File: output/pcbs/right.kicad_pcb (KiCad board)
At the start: 2 copper layers, 115.8 x 102 mm, 69 parts

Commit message: added pcbs
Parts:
- removed the ? at (166.0, 136.5)
- removed the ? at (109.0, 140.8)
- removed the ? at (109.8, 87.5)
- removed the ? at (166.0, 83.2)
- removed the ? at (147.2, 113.8)
- added ?: , HOLE_M2_TH, F.Cu at (281.5, 136.5)
- added ?: , HOLE_M2_TH, F.Cu at (338.5, 140.8)
- added ?: , HOLE_M2_TH, F.Cu at (337.8, 87.5)
- added ?: , HOLE_M2_TH, F.Cu at (281.5, 83.2)
- added ?: , HOLE_M2_TH, F.Cu at (301.0, 118.8)
- moved D2 248.1 mm to (355.3, 135.8), turned to -90 degrees
- moved D3 248.1 mm to (355.3, 118.0), turned to -90 degrees
- moved D1 247.5 mm to (355.3, 153.5), turned to -90 degrees
- moved S1 247.5 mm to (347.5, 150.0)
- moved S2 247.5 mm to (347.5, 132.2)
- moved S3 247.5 mm to (347.5, 114.5)
- moved S4 247.5 mm to (347.5, 96.8)
- moved S5 247.5 mm to (347.5, 79.0)
- moved D4 234.9 mm to (355.3, 100.2), turned to -90 degrees
- moved D5 234.9 mm to (355.3, 82.5), turned to -90 degrees
- moved D26 234.5 mm to (336.6, 77.0), turned to -90 degrees
- moved D6 213.0 mm to (336.6, 153.5), turned to -90 degrees
- moved D7 210.7 mm to (336.6, 118.0), turned to -90 degrees
- moved D8 210.7 mm to (336.6, 100.2), turned to -90 degrees
- moved S10 210.0 mm to (328.8, 79.0)
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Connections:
- net first_mod renamed mirror_first_mod
- net sixth_bottom renamed mirror_sixth_bottom
- net sixth_mod renamed mirror_sixth_mod
- net sixth_top renamed mirror_sixth_top
- net third_bottom renamed mirror_third_bottom
- net third_mod renamed mirror_third_mod
- D11 pad 1: P029 -> P002
- D11 pad 2: third_top -> mirror_third_home
- D12 pad 1: P031 -> P029
- D12 pad 2: third_num -> mirror_third_top
- D13 pad 1: P115 -> P031
- D13 pad 2: fourth_bottom -> mirror_third_num
- D14 pad 1: P002 -> P113
- D14 pad 2: fourth_home -> mirror_fourth_mod
- D15 pad 1: P031 -> P115
- D15 pad 2: fourth_num -> mirror_fourth_bottom
- D16 pad 1: P113 -> P029
- D16 pad 2: fifth_mod -> mirror_fourth_top
- D17 pad 1: P115 -> P031
- D17 pad 2: fifth_bottom -> mirror_fourth_num
- D18 pad 1: P002 -> P113
- D18 pad 2: fifth_home -> mirror_fifth_mod
- D19 pad 1: P029 -> P002
- D19 pad 2: fifth_top -> mirror_fifth_home
- D2 pad 1: P002 -> P115
- D2 pad 2: first_home -> mirror_first_bottom
- D20 pad 1: P031 -> P029
- D20 pad 2: fifth_num -> mirror_fifth_top
- D23 pad 1: P031 -> P002
- D23 pad 2: sixth_num -> mirror_sixth_home
- D25 pad 1: P002 -> P115
- D25 pad 2: sixth_home -> mirror_second_bottom
- D26 pad 1: P115 -> P031
- D26 pad 2: first_bottom -> mirror_second_num
- D27 pad 1: P031 -> P002
- D27 pad 2: first_num -> mirror_fourth_home
- D28 pad 1: P002 -> P115
- D28 pad 2: third_home -> mirror_fifth_bottom
- D29 pad 1: P113 -> P031
- D29 pad 2: fourth_mod -> mirror_fifth_num
- D3 pad 1: P029 -> P002
- D3 pad 2: first_top -> mirror_first_home
- D30 pad 1: P029 -> P031
- D30 pad 2: fourth_top -> mirror_sixth_num
- D4 pad 1: P113 -> P029
- D4 pad 2: second_mod -> mirror_first_top
- D5 pad 1: P115 -> P031
- D5 pad 2: second_bottom -> mirror_first_num
- D6 pad 1: P002 -> P113
- D6 pad 2: second_home -> mirror_second_mod
- D7 pad 1: P029 -> P002
- D7 pad 2: second_top -> mirror_second_home
- D8 pad 1: P031 -> P029
- D8 pad 2: second_num -> mirror_second_top
- S10 pad 2: second_num -> mirror_second_num
- S13 pad 2: third_home -> mirror_third_home
- S14 pad 2: third_top -> mirror_third_top
- S15 pad 2: third_num -> mirror_third_num
- S16 pad 2: fourth_mod -> mirror_fourth_mod
- S17 pad 2: fourth_bottom -> mirror_fourth_bottom
- S18 pad 2: fourth_home -> mirror_fourth_home
- S19 pad 2: fourth_top -> mirror_fourth_top
- S2 pad 2: first_bottom -> mirror_first_bottom
- S20 pad 2: fourth_num -> mirror_fourth_num
- S21 pad 2: fifth_mod -> mirror_fifth_mod
- S22 pad 2: fifth_bottom -> mirror_fifth_bottom
- S23 pad 2: fifth_home -> mirror_fifth_home
- S24 pad 2: fifth_top -> mirror_fifth_top
- S25 pad 2: fifth_num -> mirror_fifth_num
- S28 pad 2: sixth_home -> mirror_sixth_home
- S3 pad 2: first_home -> mirror_first_home
- S30 pad 2: sixth_num -> mirror_sixth_num
- S4 pad 2: first_top -> mirror_first_top
- S5 pad 2: first_num -> mirror_first_num
- S6 pad 2: second_mod -> mirror_second_mod
- S7 pad 2: second_bottom -> mirror_second_bottom
- S8 pad 2: second_home -> mirror_second_home
- S9 pad 2: second_top -> mirror_second_top
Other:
- outline, holes or cut-outs redrawn

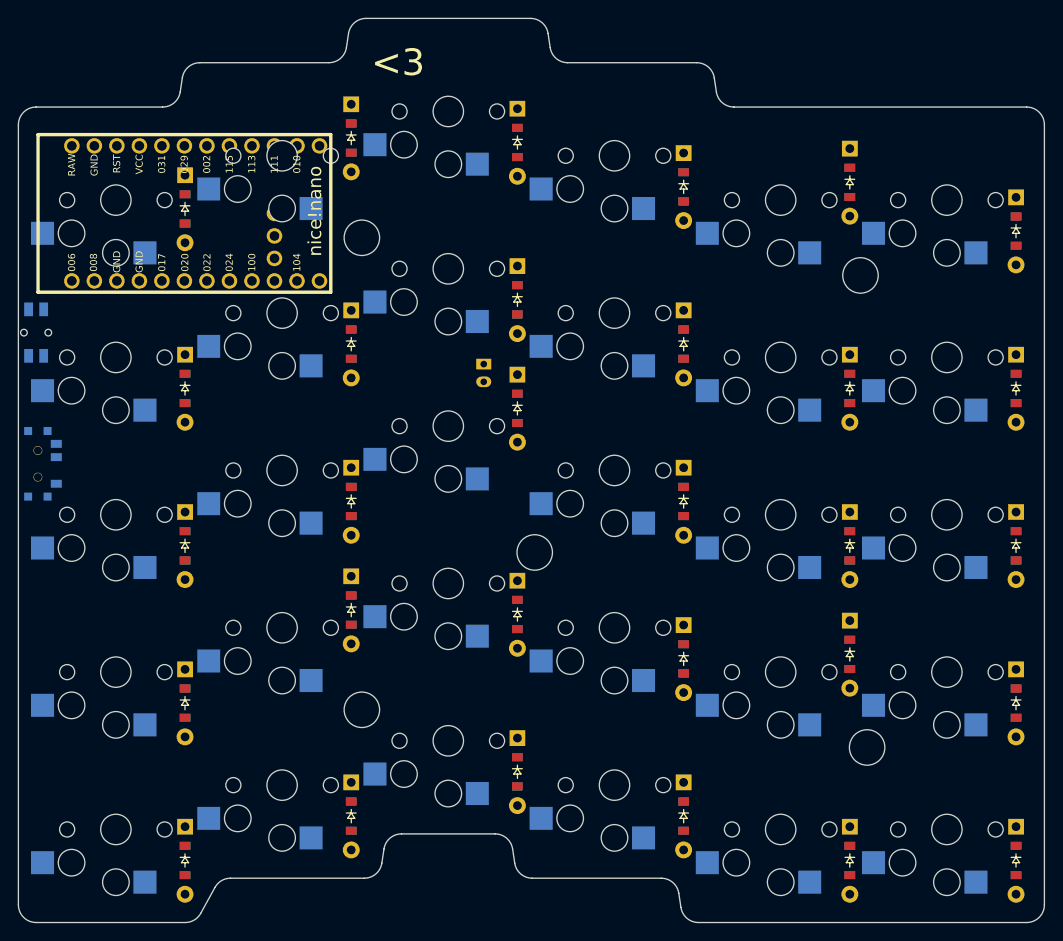
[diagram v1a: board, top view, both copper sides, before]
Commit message: changed nice!nano position
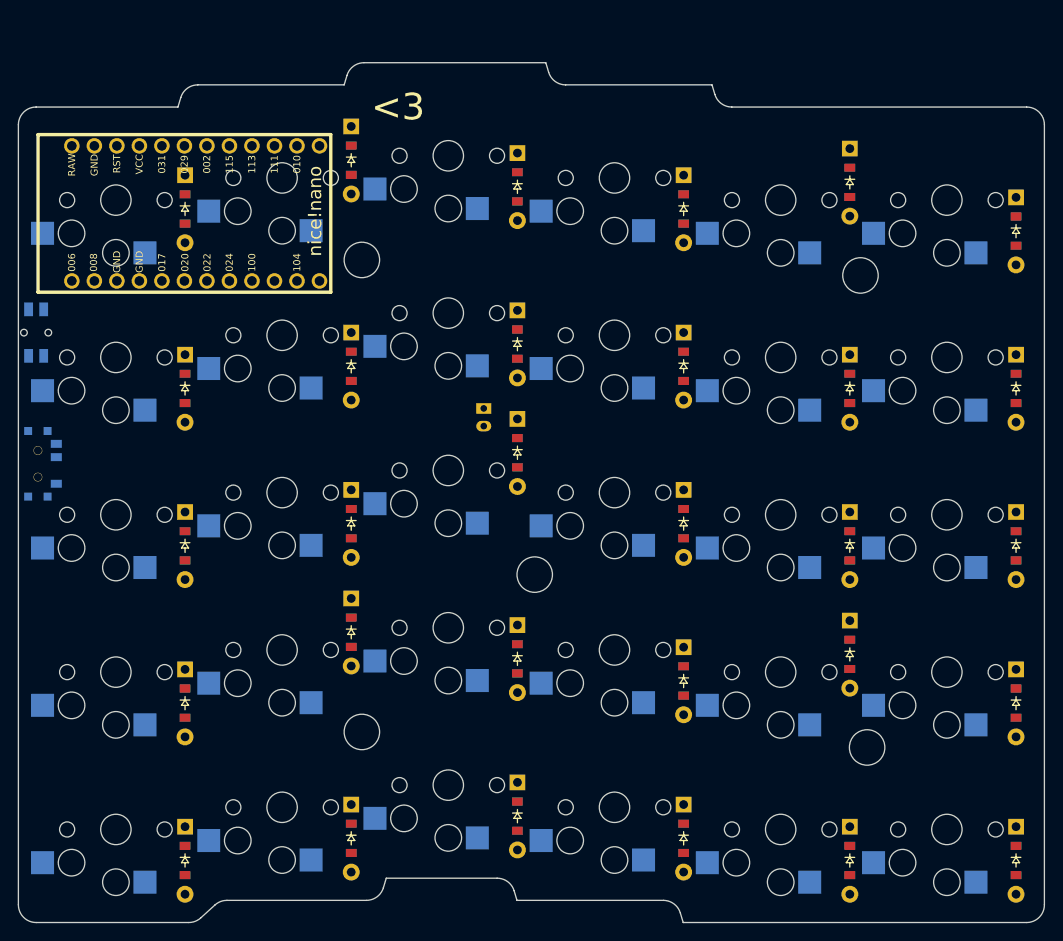
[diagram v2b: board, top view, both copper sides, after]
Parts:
- removed the ? at (281.5, 136.5)
- removed the ? at (281.5, 83.2)
- removed the ? at (301.0, 118.8)
- added ?: , HOLE_M2_TH, F.Cu at (281.5, 139.0)
- added ?: , HOLE_M2_TH, F.Cu at (281.5, 85.8)
- added ?: , HOLE_M2_TH, F.Cu at (301.0, 121.2)
- moved D14 5.00 mm to (299.1, 148.5)
- moved D15 5.00 mm to (299.1, 130.8)
- moved D16 5.00 mm to (299.1, 95.2)
- moved D17 5.00 mm to (299.1, 77.5)
- moved D27 5.00 mm to (299.1, 107.5)
- moved JST1 5.00 mm to (295.2, 103.5)
- moved S16 5.00 mm to (291.2, 145.0)
- moved S17 5.00 mm to (291.2, 127.2)
- moved S18 5.00 mm to (291.2, 109.5)
- moved S19 5.00 mm to (291.2, 91.8)
- moved S20 5.00 mm to (291.2, 74.0)
- moved D10 2.50 mm to (317.8, 133.2)
- moved D11 2.50 mm to (317.8, 115.5)
- moved D12 2.50 mm to (317.8, 97.8)
- moved D13 2.50 mm to (317.8, 80.0)
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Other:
- board size 115.8 x 102 mm -> 115.8 x 97 mm

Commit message: added readme
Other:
- board text added: "WHISPER"
- board text removed: "<3"
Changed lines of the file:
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@@
       (at 301 121.25 0)
       (pad "" np_thru_hole circle (at 0 0 90) (size 4.0 4.0) (drill 4.0) (layers *.Cu *.Mask F.SilkS) (clearance 0.3)))
-            (gr_text "<3" (at 282.55 68.5 0) (layer F.SilkS)
+            (gr_text "WHISPER" (at 282.55 68.5 0) (layer F.SilkS)
                 (effects (font (size 3 3) (thickness 0.4) ) (justify left))
             )
